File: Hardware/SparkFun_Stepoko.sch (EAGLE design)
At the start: 178 parts, among them J1 AVR ISP, Q1 16MHZ, Q2 100A/100V, U1 ATMEGA328, U10 +12v, U2 FT232RLSSOP, U3 74LVC1G04, U4 LM25011, U5 DRV8811, U6 74HC7014D, U7 7432SE, U8 DRV8811, U9 DRV8811

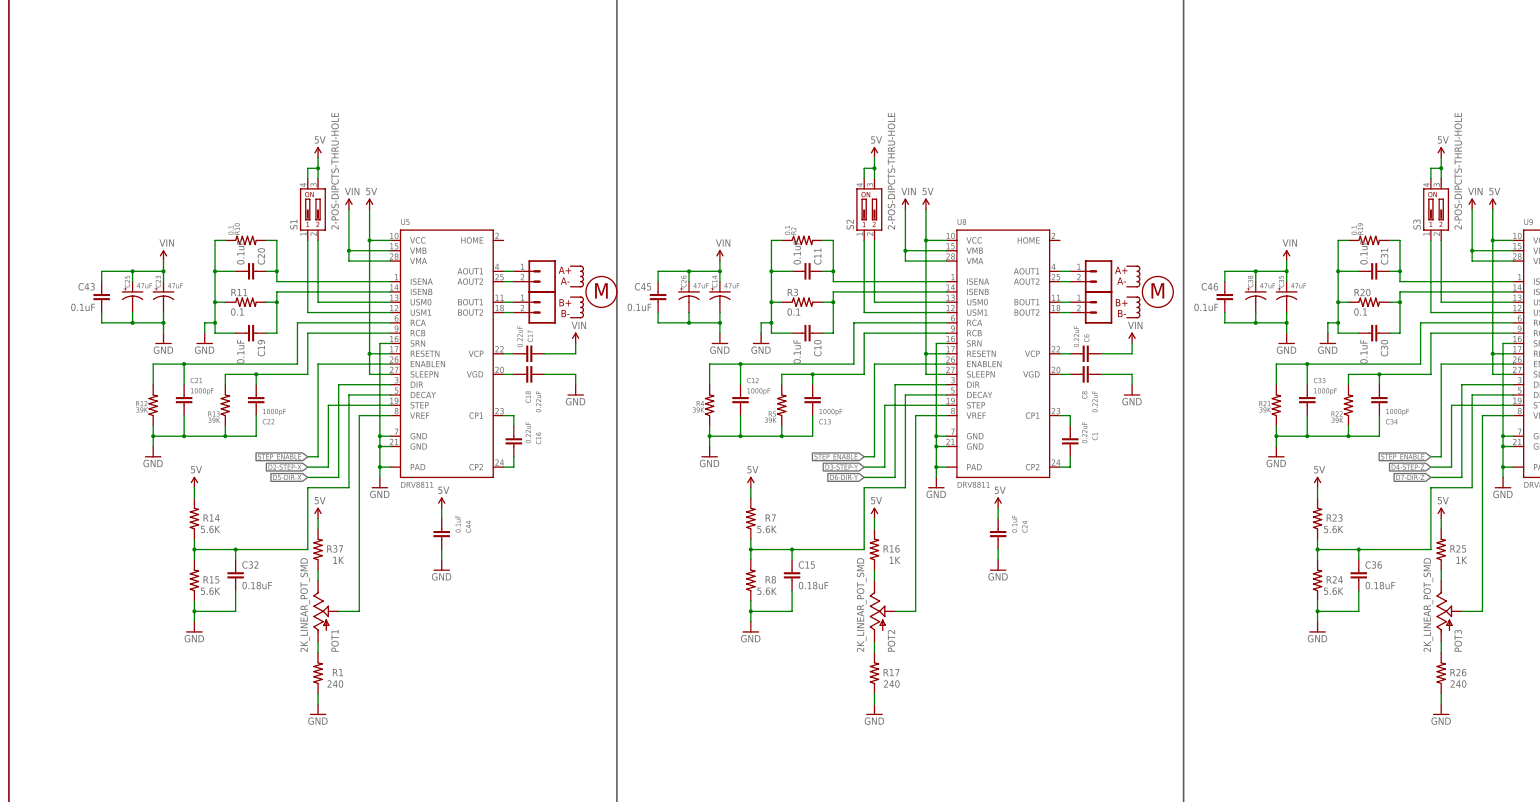
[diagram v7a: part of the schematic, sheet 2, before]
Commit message: fixed current limit resistor values
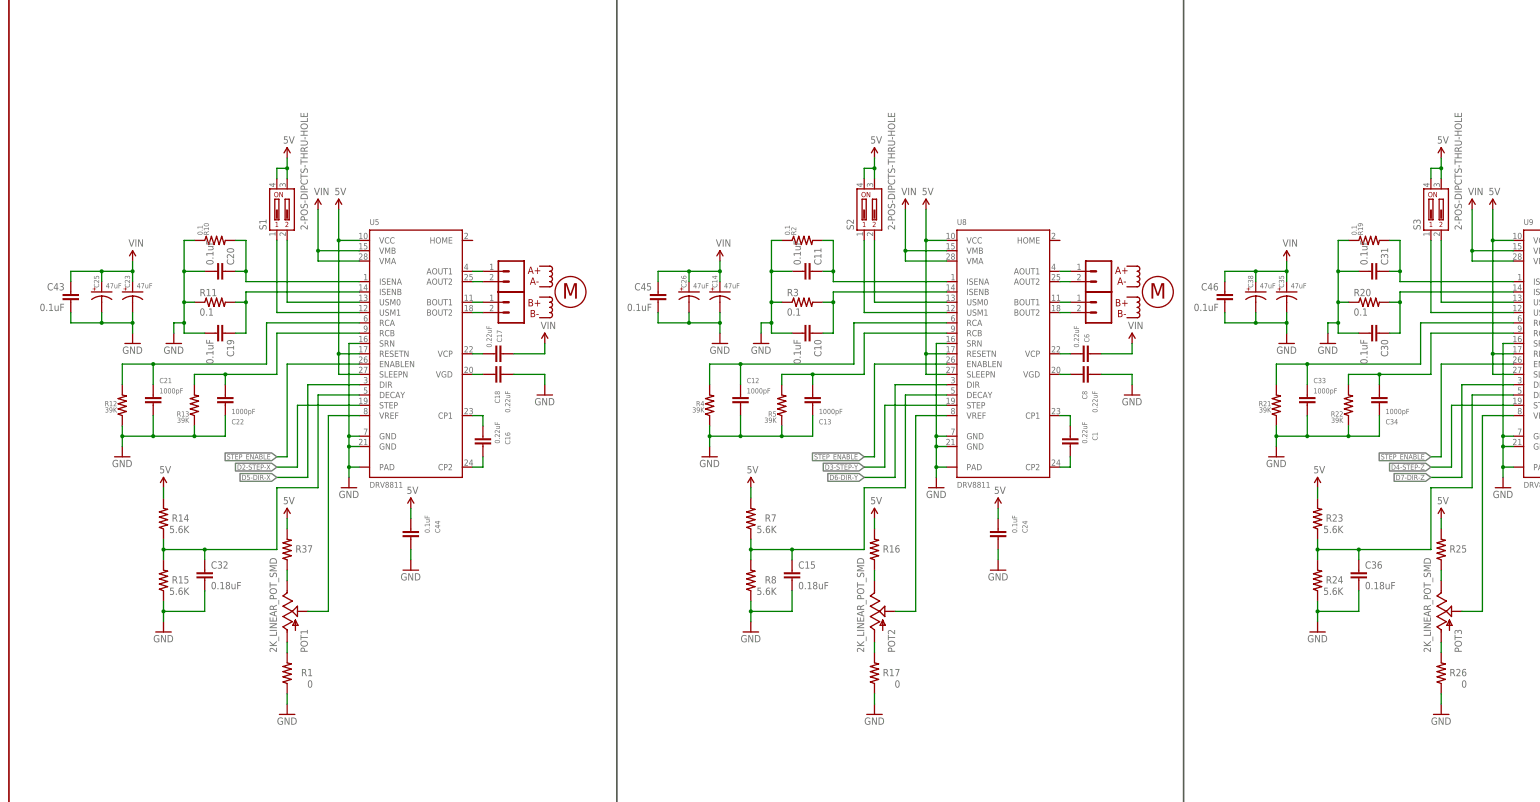
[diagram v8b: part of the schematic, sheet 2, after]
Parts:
- R1, R17, R26: value 240 -> 0; device SparkFun-Resistors:240OHM1/10W1%(0603) -> SparkFun-Resistors:0OHM-1/10W-5%(0603)
- R16, R25, R37: value 1K -> 3.3K; device SparkFun-Resistors:1KOHM-1/10W-1%(0603) -> SparkFun-Resistors:3.3KOHM1/10W1%(0603)
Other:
- moved on the sheet: C16, C17, C18, C19, C20, C21, C22, C23, C25, C32, C43, C44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
